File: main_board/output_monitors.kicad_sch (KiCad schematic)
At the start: 84 parts, among them U14 TLV2172IDR, U17 TLV2172IDR, U18 TLV2172IDR, U4 TLV2172IDR

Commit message: Version 0.03
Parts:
- added SO10, SO11, SO12, SO13, SO14, SO15, SO16, SO17, SO18, SO19, SO20, SO21, SO22, SO23, SO24, SO9: LED_Standoff, symbol greenface:LED_Standoff
- R121, R122, R123, R124, R93, R94, R95, R96: value 10K -> 56K;  LCSC Part # C138260 -> C137420; Digi-Key Part 13-RC0805JR-1010KLCT-ND -> 311-56KARCT-ND
- U14, U17, U18, U4: value TLV2172IDR -> TL072CDR;  LCSC Part # C129149 -> C67473
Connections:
- net +12V: now also U14.8 (V+), U17.8 (V+), U18.8 (V+), U4.8 (V+); no longer U14.4 (V-), U17.4 (V-), U18.4 (V-), U4.4 (V-)
- net -12V: now also U14.4 (V-), U17.4 (V-), U18.4 (V-), U4.4 (V-); no longer U14.8 (V+), U17.8 (V+), U18.8 (V+), U4.8 (V+)

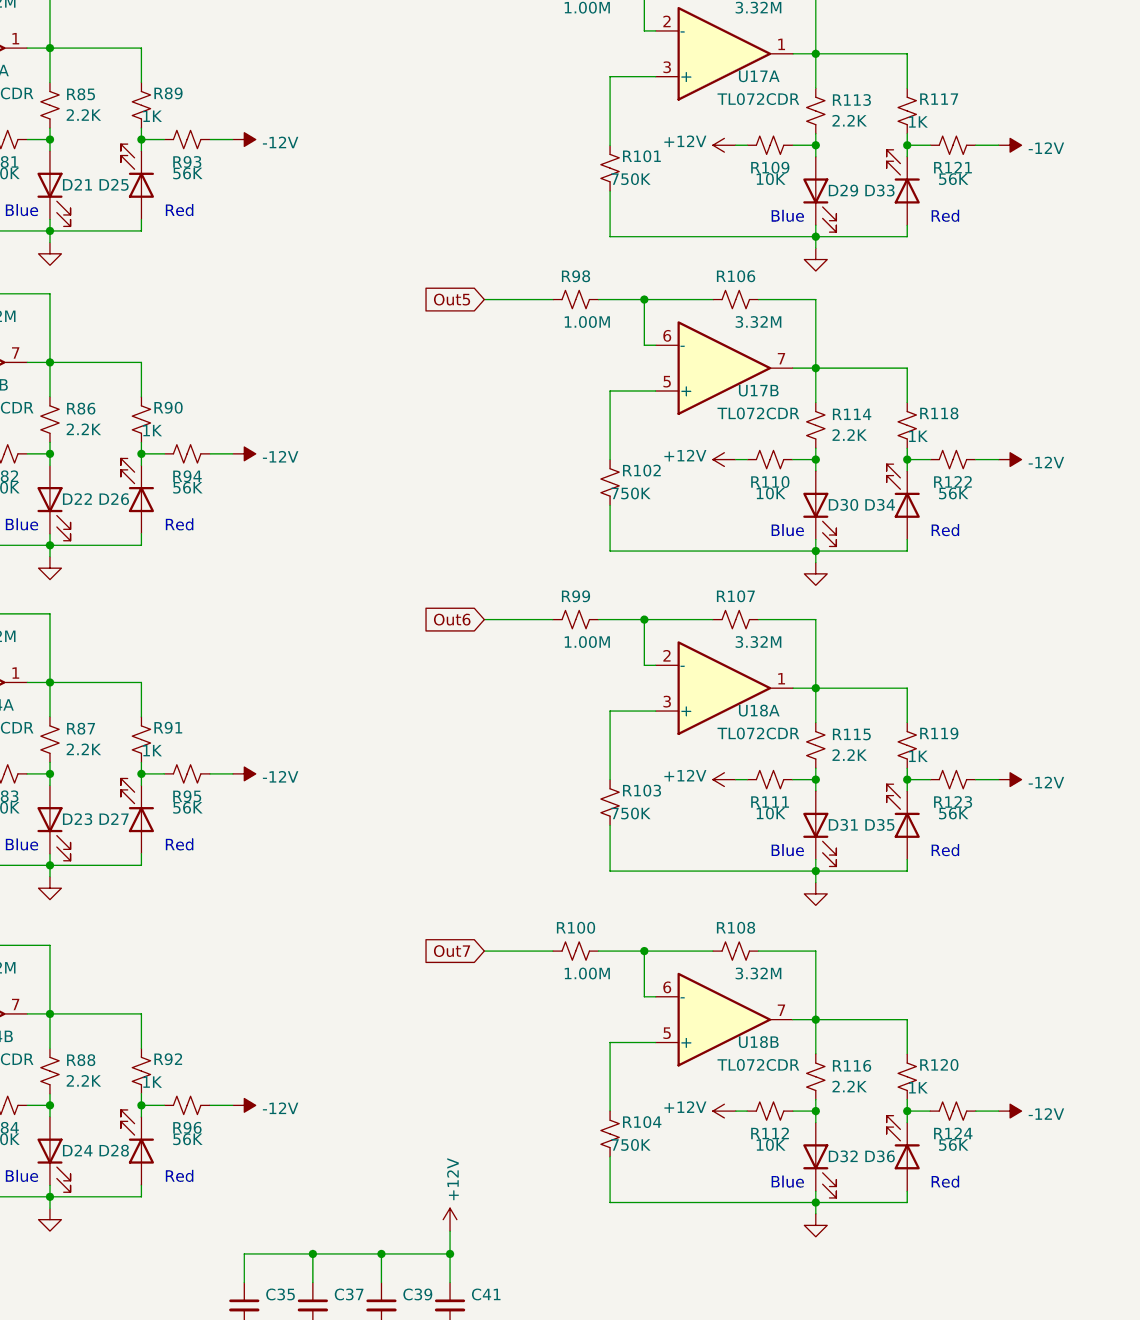
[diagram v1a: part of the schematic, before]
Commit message: Software v2.2
Removes unneeded files.
Adds pre-flight handler in WiFi do_server();
Removes debug printouts.
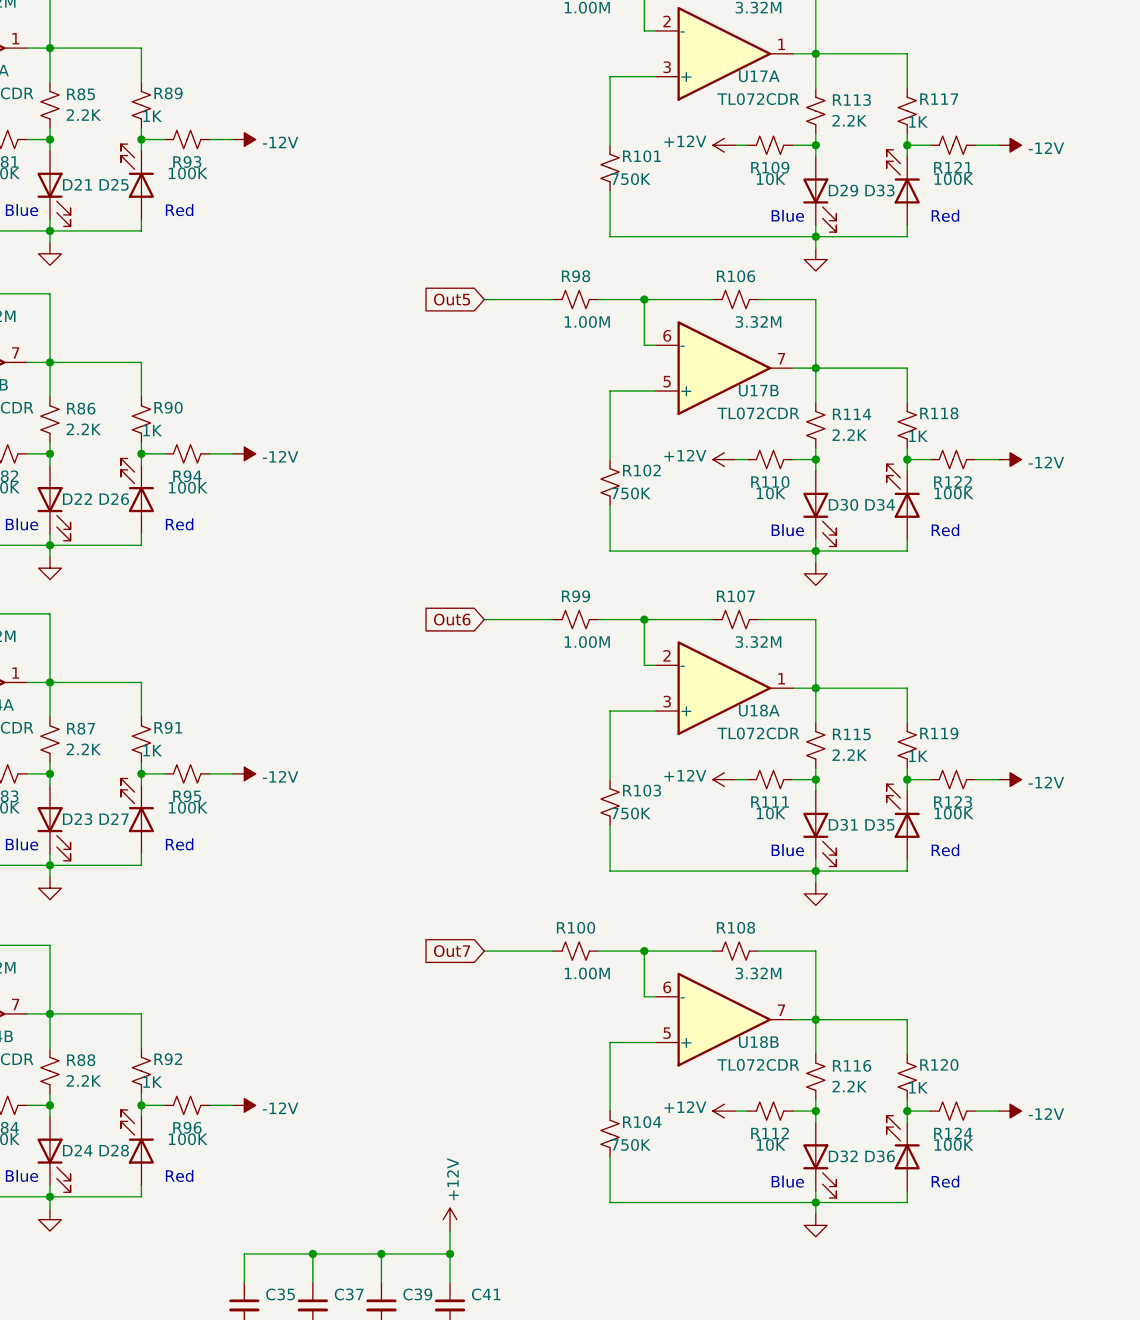
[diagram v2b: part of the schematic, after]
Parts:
- R121, R122, R123, R124, R93, R94, R95, R96: value 56K -> 100K;  LCSC Part # C137420 -> C100049
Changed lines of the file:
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@@
     (in_bom yes) (on_board yes)
     (property "Reference" "R96" (id 0) (at 121.285 148.59 90))
-    (property "Value" "56K" (id 1) (at 121.285 149.86 90))
+    (property "Value" "100K" (id 1) (at 121.285 149.86 90))
     (property "Footprint" "Resistor_SMD:R_0805_2012Metric_Pad1.20x1.40mm_HandSolder" (id 2) (at 121.285 146.05 0)
       (effects (font (size 1.27 1.27)) hide)
@@
       (effects (font (size 1.27 1.27)) hide)
     )
-    (property " LCSC Part #" "C137420" (id 5) (at 121.285 146.05 0)
+    (property " LCSC Part #" "C100049" (id 5) (at 121.285 146.05 0)
       (effects (font (size 1.27 1.27)) hide)
     )
@@
     (in_bom yes) (on_board yes)
     (property "Reference" "R95" (id 0) (at 121.285 111.76 90))
-    (property "Value" "56K" (id 1) (at 121.285 113.03 90))
+    (property "Value" "100K" (id 1) (at 121.285 113.03 90))
     (property "Footprint" "Resistor_SMD:R_0805_2012Metric_Pad1.20x1.40mm_HandSolder" (id 2) (at 121.285 109.22 0)
       (effects (font (size 1.27 1.27)) hide)
@@
       (effects (font (size 1.27 1.27)) hide)
     )
-    (property " LCSC Part #" "C137420" (id 5) (at 121.285 109.22 0)
+    (property " LCSC Part #" "C100049" (id 5) (at 121.285 109.22 0)
       (effects (font (size 1.27 1.27)) hide)
     )
@@
     (in_bom yes) (on_board yes)
     (property "Reference" "R124" (id 0) (at 206.375 149.225 90))
-    (property "Value" "56K" (id 1) (at 206.375 150.495 90))
+    (property "Value" "100K" (id 1) (at 206.375 150.495 90))
     (property "Footprint" "Resistor_SMD:R_0805_2012Metric_Pad1.20x1.40mm_HandSolder" (id 2) (at 206.375 146.685 0)
       (effects (font (size 1.27 1.27)) hide)
@@
       (effects (font (size 1.27 1.27)) hide)
     )
-    (property " LCSC Part #" "C137420" (id 5) (at 206.375 146.685 0)
+    (property " LCSC Part #" "C100049" (id 5) (at 206.375 146.685 0)
       (effects (font (size 1.27 1.27)) hide)
     )
@@
     (in_bom yes) (on_board yes)
     (property "Reference" "R121" (id 0) (at 206.375 41.91 90))
-    (property "Value" "56K" (id 1) (at 206.375 43.18 90))
+    (property "Value" "100K" (id 1) (at 206.375 43.18 90))
     (property "Footprint" "Resistor_SMD:R_0805_2012Metric_Pad1.20x1.40mm_HandSolder" (id 2) (at 206.375 39.37 0)
       (effects (font (size 1.27 1.27)) hide)
@@
       (effects (font (size 1.27 1.27)) hide)
     )
-    (property " LCSC Part #" "C137420" (id 5) (at 206.375 39.37 0)
+    (property " LCSC Part #" "C100049" (id 5) (at 206.375 39.37 0)
       (effects (font (size 1.27 1.27)) hide)
     )
@@
     (in_bom yes) (on_board yes)
     (property "Reference" "R123" (id 0) (at 206.375 112.395 90))
-    (property "Value" "56K" (id 1) (at 206.375 113.665 90))
+    (property "Value" "100K" (id 1) (at 206.375 113.665 90))
     (property "Footprint" "Resistor_SMD:R_0805_2012Metric_Pad1.20x1.40mm_HandSolder" (id 2) (at 206.375 109.855 0)
       (effects (font (size 1.27 1.27)) hide)
@@
       (effects (font (size 1.27 1.27)) hide)
     )
-    (property " LCSC Part #" "C137420" (id 5) (at 206.375 109.855 0)
+    (property " LCSC Part #" "C100049" (id 5) (at 206.375 109.855 0)
       (effects (font (size 1.27 1.27)) hide)
     )
@@
     (in_bom yes) (on_board yes)
     (property "Reference" "R94" (id 0) (at 121.285 76.2 90))
-    (property "Value" "56K" (id 1) (at 121.285 77.47 90))
+    (property "Value" "100K" (id 1) (at 121.285 77.47 90))
     (property "Footprint" "Resistor_SMD:R_0805_2012Metric_Pad1.20x1.40mm_HandSolder" (id 2) (at 121.285 73.66 0)
       (effects (font (size 1.27 1.27)) hide)
@@
       (effects (font (size 1.27 1.27)) hide)
     )
-    (property " LCSC Part #" "C137420" (id 5) (at 121.285 73.66 0)
+    (property " LCSC Part #" "C100049" (id 5) (at 121.285 73.66 0)
       (effects (font (size 1.27 1.27)) hide)
     )
@@
     (in_bom yes) (on_board yes)
     (property "Reference" "R93" (id 0) (at 121.285 41.275 90))
-    (property "Value" "56K" (id 1) (at 121.285 42.545 90))
+    (property "Value" "100K" (id 1) (at 121.285 42.545 90))
     (property "Footprint" "Resistor_SMD:R_0805_2012Metric_Pad1.20x1.40mm_HandSolder" (id 2) (at 121.285 38.735 0)
       (effects (font (size 1.27 1.27)) hide)
@@
       (effects (font (size 1.27 1.27)) hide)
     )
-    (property " LCSC Part #" "C137420" (id 5) (at 121.285 38.735 0)
+    (property " LCSC Part #" "C100049" (id 5) (at 121.285 38.735 0)
       (effects (font (size 1.27 1.27)) hide)
     )
@@
     (in_bom yes) (on_board yes)
     (property "Reference" "R122" (id 0) (at 206.375 76.835 90))
-    (property "Value" "56K" (id 1) (at 206.375 78.105 90))
+    (property "Value" "100K" (id 1) (at 206.375 78.105 90))
     (property "Footprint" "Resistor_SMD:R_0805_2012Metric_Pad1.20x1.40mm_HandSolder" (id 2) (at 206.375 74.295 0)
       (effects (font (size 1.27 1.27)) hide)
@@
       (effects (font (size 1.27 1.27)) hide)
     )
-    (property " LCSC Part #" "C137420" (id 5) (at 206.375 74.295 0)
-      (effects (font (size 1.27 1.27)) hide)
-    )
+    (property " LCSC Part #" "C100049" (id 5) (at 206.375 74.295 0)
+      (effects (font (size 1.27 1.27)) hide)
+    )

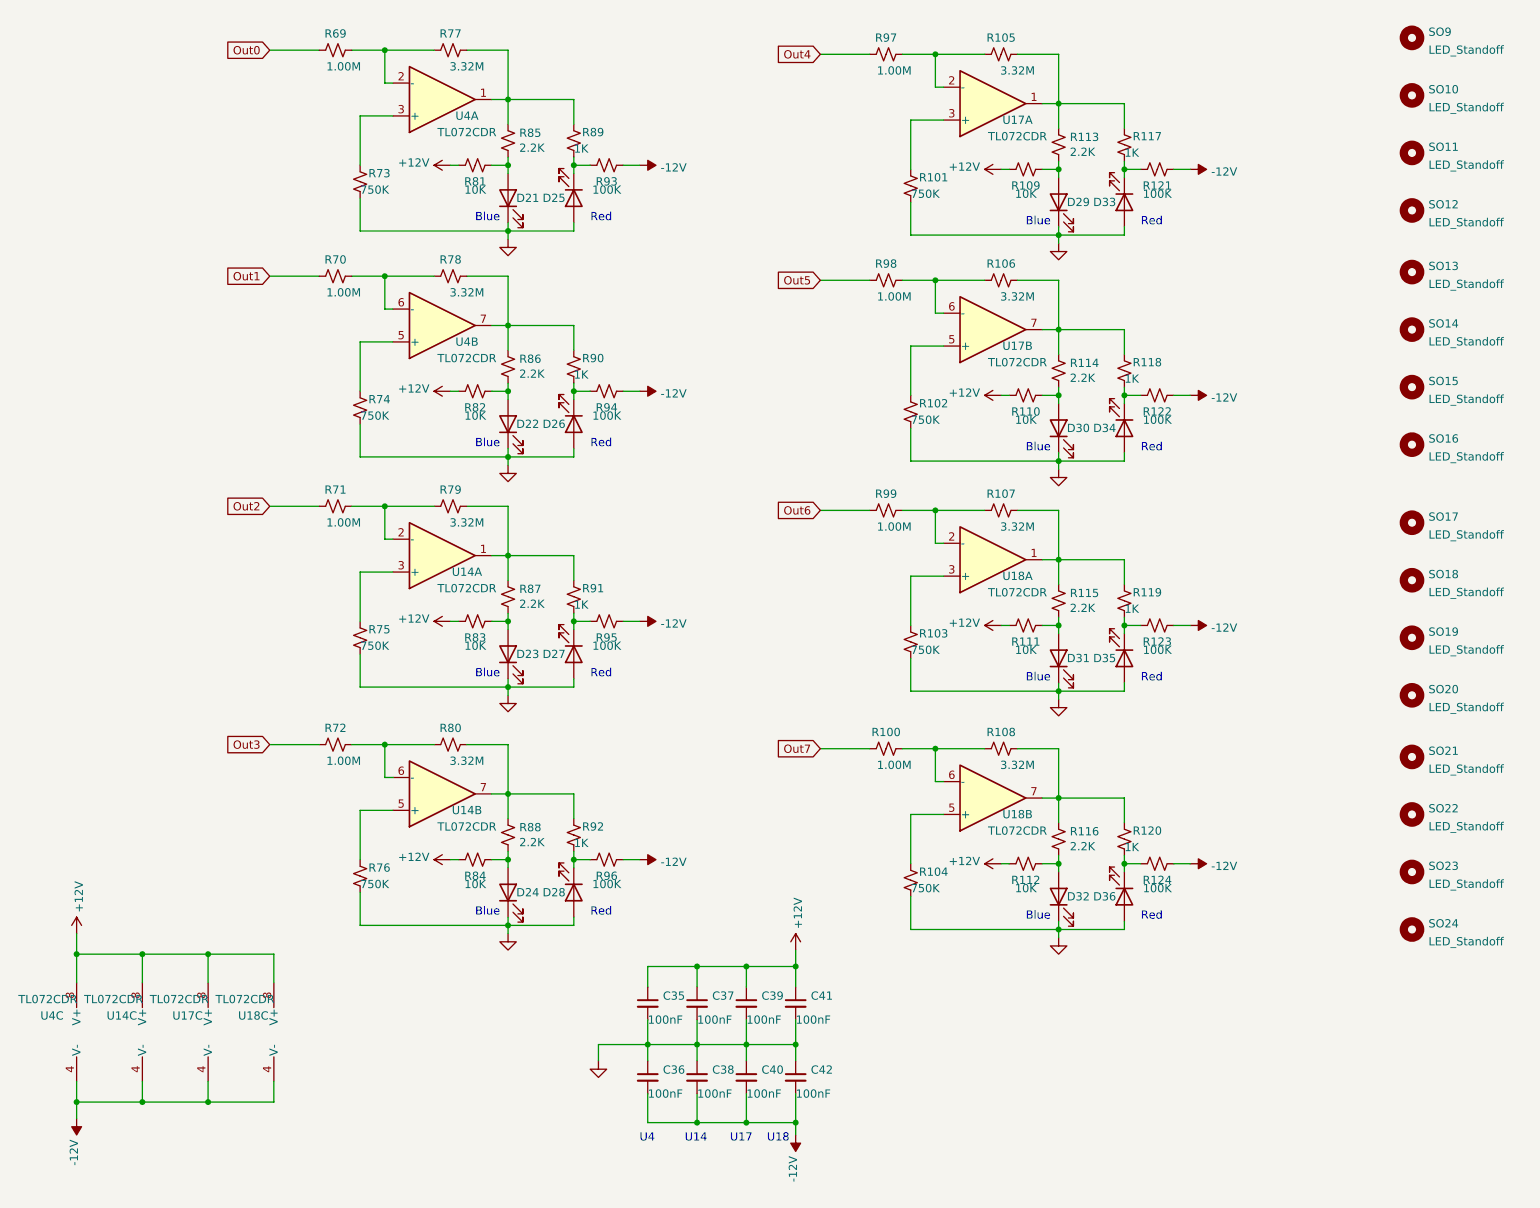
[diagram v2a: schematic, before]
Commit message: Updates monitor circuitry. Sets outputs on init().
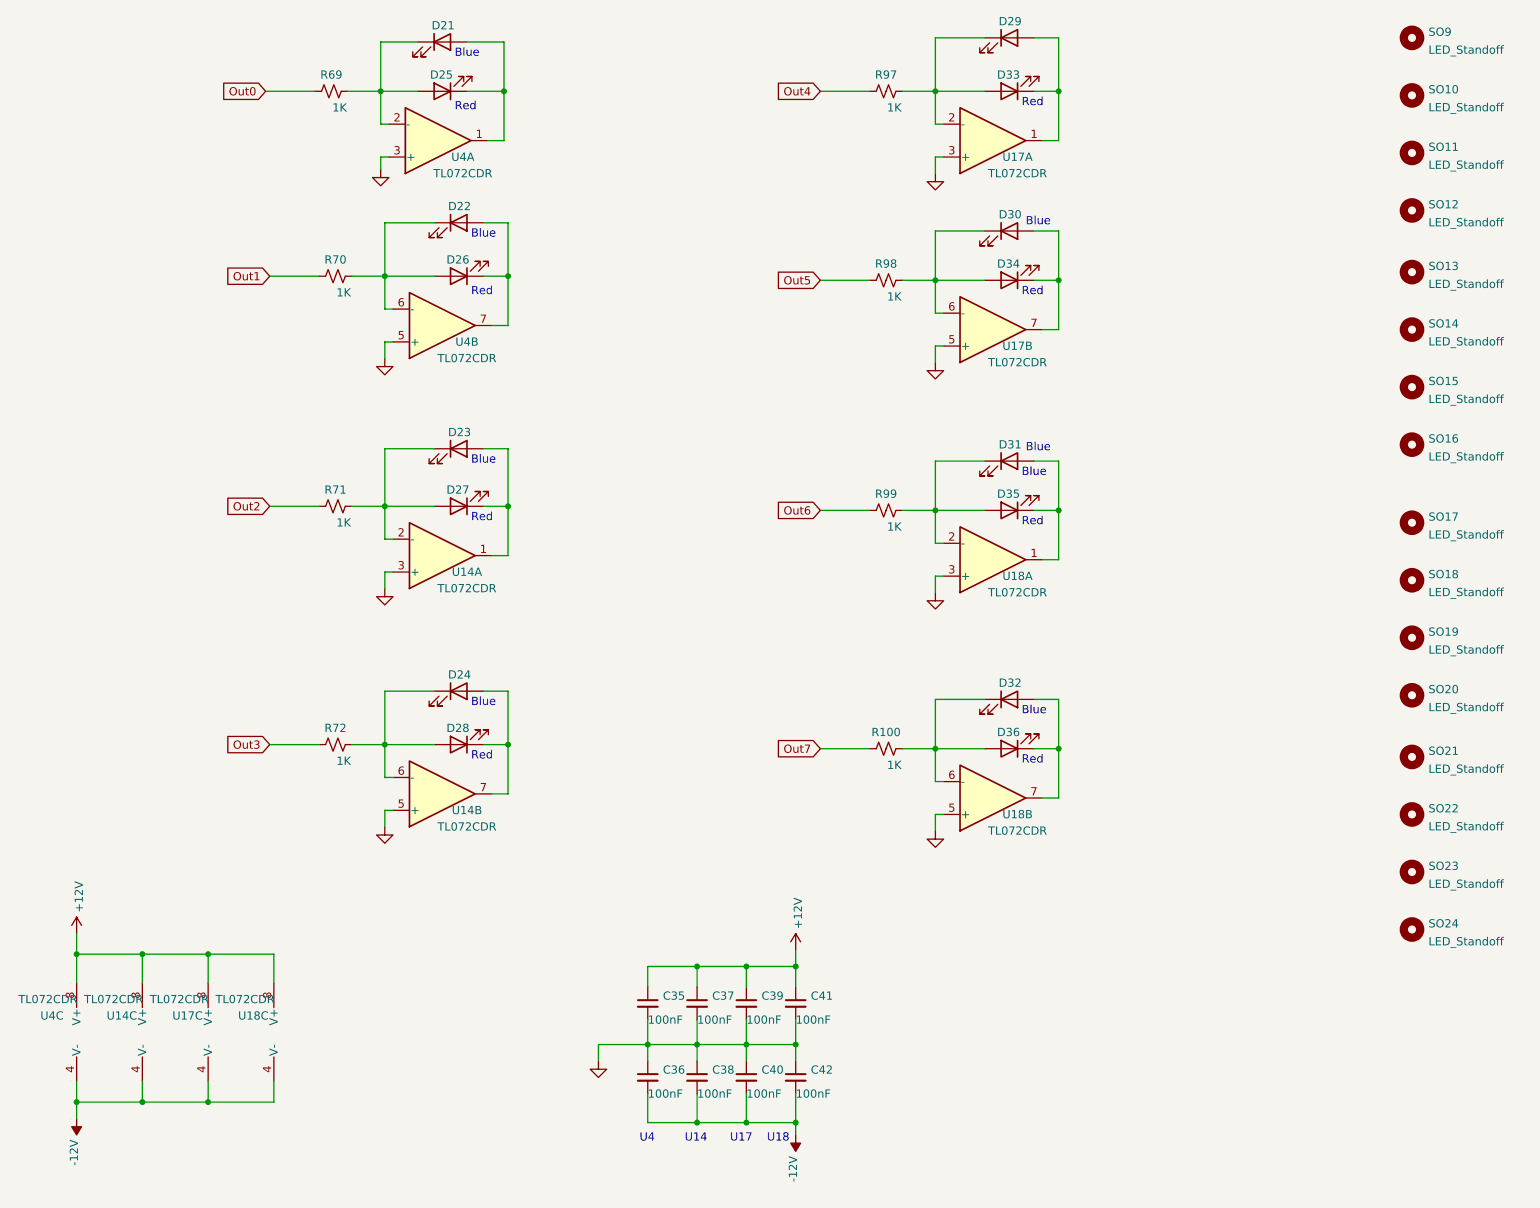
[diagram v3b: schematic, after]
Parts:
- removed R101, R102, R103, R104, R73, R74, R75, R76: 750K, Resistor_SMD:R_0805_2012Metric_Pad1.20x1.40mm_HandSolder, symbol Device:R_Small_US
- removed R105, R106, R107, R108, R77, R78, R79, R80: 3.32M, Resistor_SMD:R_0805_2012Metric_Pad1.20x1.40mm_HandSolder, symbol Device:R_Small_US
- removed R109, R110, R111, R112, R81, R82, R83, R84: 10K, Resistor_SMD:R_0805_2012Metric_Pad1.20x1.40mm_HandSolder, symbol Device:R_Small_US
- removed R113, R114, R115, R116, R85, R86, R87, R88: 2.2K, Resistor_SMD:R_0805_2012Metric_Pad1.20x1.40mm_HandSolder, symbol Device:R_Small_US
- removed R117, R118, R119, R120, R89, R90, R91, R92: 1K, Resistor_SMD:R_0805_2012Metric_Pad1.20x1.40mm_HandSolder, symbol Device:R_Small_US
- removed R121, R122, R123, R124, R93, R94, R95, R96: 100K, Resistor_SMD:R_0805_2012Metric_Pad1.20x1.40mm_HandSolder, symbol Device:R_Small_US
- R100, R69, R70, R71, R72, R97, R98, R99: value 1.00M -> 1K;  LCSC Part # C107700 -> C17513; Digi-Key Part 311-1.00MCRCT-ND -> 311-10KARCT-ND
- U14, U17, U18, U4:  LCSC Part # C67473 -> C6961
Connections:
- net GND: now also U14.3 (+), U14.5 (+), U17.3 (+), U17.5 (+), U18.3 (+), U18.5 (+), U4.3 (+), U4.5 (+); no longer D21.1 (K), D22.1 (K), D23.1 (K), D24.1 (K), D25.2 (A), D26.2 (A), D27.2 (A), D28.2 (A), D29.1 (K), D30.1 (K), D31.1 (K), D32.1 (K), D33.2 (A), D34.2 (A), D35.2 (A), D36.2 (A)
- net at U18.7: now also D32.2 (A), D36.1 (K)
- net at R72.2, U14.6 (-): now also D24.1 (K), D28.2 (A)
- net at D24.2 (A): now also D28.1 (K), U14.7
- net at R100.2, U18.6 (-): now also D32.1 (K), D36.2 (A)
- net at U17.1: now also D29.2 (A), D33.1 (K)
- net at R97.2, U17.2 (-): now also D29.1 (K), D33.2 (A)
- net at D22.2 (A): now also D26.1 (K), U4.7
- net at R69.2, U4.2 (-): now also D21.1 (K), D25.2 (A)
- net at D27.1 (K): now also D23.2 (A), U14.1
- net at D31.2 (A): now also D35.1 (K), U18.1
- net at R99.2, U18.2 (-): now also D31.1 (K), D35.2 (A)
- net at U17.7: now also D30.2 (A), D34.1 (K)
- net at R98.2, U17.6 (-): now also D30.1 (K), D34.2 (A)
- net at R70.2, U4.6 (-): now also D22.1 (K), D26.2 (A)
- net at U4.1: now also D21.2 (A), D25.1 (K)
- net at R71.2, U14.2 (-): now also D23.1 (K), D27.2 (A)
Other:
- moved on the sheet: D21, D22, D23, D24, D25, D26, D27, D28, D29, D30, D31, D32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
